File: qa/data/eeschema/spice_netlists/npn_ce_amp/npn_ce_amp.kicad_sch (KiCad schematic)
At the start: 10 parts

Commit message: Sim: Bugfixes, mostly for MS Windows compilation errors
Unfortunately, Windows headers define a lot of macros for common words,
so we had to rename some enums to not collide.

We also fix some of the many bugs related to the new simulation
architecture and the Spice Model Editor dialog.
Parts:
- Q1: Model_Device NPN -> (none); Model_Library npn.lib.spice -> (none); Model_Name NPN -> (none); Model_Pins 1 2 3 -> (none); Model_Type GUMMELPOON -> (none); Sim_Device (none) -> NPN; Sim_Library (none) -> npn.lib.spice; Sim_Name (none) -> NPN; Sim_Pins (none) -> 1 2 3; Sim_Type (none) -> GUMMELPOON
- V1: Model_Device V -> (none); Model_Params dc=9 -> (none); Model_Pins 1 2 -> (none); Model_Type DC -> (none); Sim_Device (none) -> V; Sim_Params (none) -> dc=9; Sim_Pins (none) -> 1 2; Sim_Type (none) -> DC
- V2: Model_Device V -> (none); Model_Params dc=0 ampl=10m f=10k -> (none); Model_Pins 1 2 -> (none); Model_Type SIN -> (none); Sim_Device (none) -> V; Sim_Params (none) -> dc=0 ampl=10m f=10k; Sim_Pins (none) -> 1 2; Sim_Type (none) -> SIN
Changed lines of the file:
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@@
       (effects (font (size 1.27 1.27)) hide)
     )
-    (property "Model_Name" "NPN" (id 4) (at 142.875 92.71 0)
+    (property "Sim_Name" "NPN" (id 4) (at 142.875 92.71 0)
       (effects (font (size 1.27 1.27)))
     )
-    (property "Model_Library" "npn.lib.spice" (id 5) (at 135.89 88.9 0)
+    (property "Sim_Library" "npn.lib.spice" (id 5) (at 135.89 88.9 0)
       (effects (font (size 1.27 1.27)) hide)
     )
-    (property "Model_Device" "NPN" (id 6) (at 135.89 88.9 0)
+    (property "Sim_Device" "NPN" (id 6) (at 135.89 88.9 0)
       (effects (font (size 1.27 1.27)) hide)
     )
-    (property "Model_Type" "GUMMELPOON" (id 7) (at 135.89 88.9 0)
+    (property "Sim_Type" "GUMMELPOON" (id 7) (at 135.89 88.9 0)
       (effects (font (size 1.27 1.27)) hide)
     )
-    (property "Model_Pins" "1 2 3" (id 8) (at 135.89 88.9 0)
+    (property "Sim_Pins" "1 2 3" (id 8) (at 135.89 88.9 0)
       (effects (font (size 1.27 1.27)) hide)
     )
@@
       (effects (font (size 1.27 1.27)) hide)
     )
-    (property "Model_Device" "V" (id 4) (at 114.3 93.98 0)
+    (property "Sim_Device" "V" (id 4) (at 114.3 93.98 0)
       (effects (font (size 1.27 1.27)) hide)
     )
-    (property "Model_Type" "SIN" (id 5) (at 114.3 93.98 0)
+    (property "Sim_Type" "SIN" (id 5) (at 114.3 93.98 0)
       (effects (font (size 1.27 1.27)) hide)
     )
-    (property "Model_Pins" "1 2" (id 6) (at 114.3 93.98 0)
+    (property "Sim_Pins" "1 2" (id 6) (at 114.3 93.98 0)
       (effects (font (size 1.27 1.27)) hide)
     )
-    (property "Model_Params" "dc=0 ampl=10m f=10k" (id 7) (at 114.3 106.68 0)
+    (property "Sim_Params" "dc=0 ampl=10m f=10k" (id 7) (at 114.3 106.68 0)
       (effects (font (size 1.27 1.27)))
     )
@@
       (effects (font (size 1.27 1.27)) hide)
     )
-    (property "Model_Device" "V" (id 4) (at 101.6 85.09 0)
+    (property "Sim_Device" "V" (id 4) (at 101.6 85.09 0)
       (effects (font (size 1.27 1.27)) hide)
     )
-    (property "Model_Type" "DC" (id 5) (at 101.6 85.09 0)
+    (property "Sim_Type" "DC" (id 5) (at 101.6 85.09 0)
       (effects (font (size 1.27 1.27)) hide)
     )
-    (property "Model_Pins" "1 2" (id 6) (at 101.6 85.09 0)
+    (property "Sim_Pins" "1 2" (id 6) (at 101.6 85.09 0)
       (effects (font (size 1.27 1.27)) hide)
     )
-    (property "Model_Params" "dc=9" (id 7) (at 107.95 87.63 0)
+    (property "Sim_Params" "dc=9" (id 7) (at 107.95 87.63 0)
       (effects (font (size 1.27 1.27)))
     )

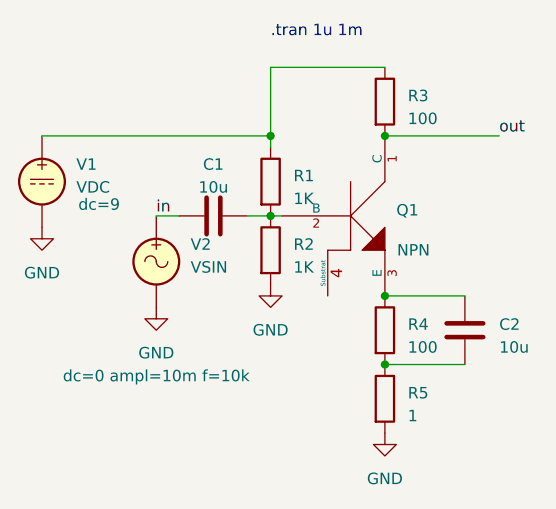
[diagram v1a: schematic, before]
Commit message: Sim: Only store device type in reference, not full model type
Instead of Reference="VSIN1", Value="dc=1 ampl=2 f=3", it's now
Reference="V1", Value="SIN dc=1 ampl=2 f=3".
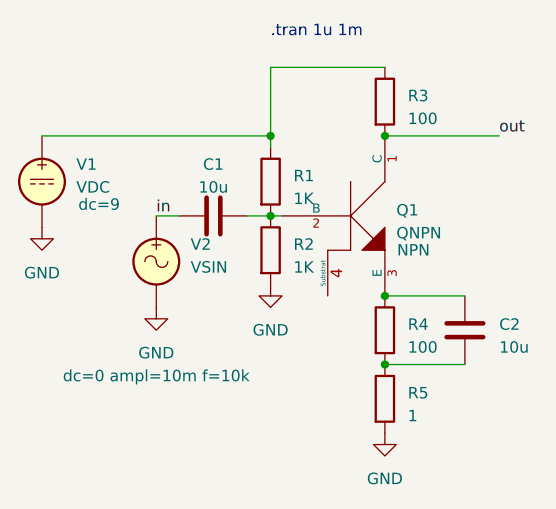
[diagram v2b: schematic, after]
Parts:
- Q1: value (none) -> QNPN
- V1: Sim_Type DC -> (none)

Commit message: Sim: Remove inference from Reference and Value
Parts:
- C1, C2: Sim_Device (none) -> C
- R1, R2, R3, R4, R5: Sim_Device (none) -> R
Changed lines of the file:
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@@
+      (effects (font (size 1.27 1.27)) hide)
+    )
+    (property "Sim_Device" "C" (at 120.65 88.9 90)
       (effects (font (size 1.27 1.27)) hide)
     )
@@
       (effects (font (size 1.27 1.27)) hide)
     )
+    (property "Sim_Device" "C" (at 148.59 101.6 0)
+      (effects (font (size 1.27 1.27)) hide)
+    )
     (pin "1")
     (pin "2")
@@
     )
     (property "Datasheet" "~" (at 139.7 76.2 0)
+      (effects (font (size 1.27 1.27)) hide)
+    )
+    (property "Sim_Device" "R" (at 139.7 76.2 0)
       (effects (font (size 1.27 1.27)) hide)
     )
@@
       (effects (font (size 1.27 1.27)) hide)
     )
+    (property "Sim_Device" "R" (at 139.7 101.6 0)
+      (effects (font (size 1.27 1.27)) hide)
+    )
     (pin "1")
     (pin "2")
@@
       (effects (font (size 1.27 1.27)) hide)
     )
+    (property "Sim_Device" "R" (at 127 85.09 0)
+      (effects (font (size 1.27 1.27)) hide)
+    )
     (pin "1")
     (pin "2")
@@
       (effects (font (size 1.27 1.27)) hide)
     )
+    (property "Sim_Device" "R" (at 139.7 109.22 0)
+      (effects (font (size 1.27 1.27)) hide)
+    )
     (pin "1")
     (pin "2")
@@
       (effects (font (size 1.27 1.27)) hide)
     )
+    (property "Sim_Device" "R" (at 127 92.71 0)
+      (effects (font (size 1.27 1.27)) hide)
+    )

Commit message: Sim: Rename Sim_* fields to Sim.*
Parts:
- C1, C2: Sim_Device C -> (none)
- Q1: Sim_Device NPN -> (none); Sim_Pins 1 2 3 -> (none); Sim_Type GUMMELPOON -> (none)
- R1, R2, R3, R4, R5: Sim_Device R -> (none)
- V1: Sim_Device V -> (none); Sim_Params dc=9 -> (none); Sim_Pins 1 2 -> (none)
- V2: Sim_Device V -> (none); Sim_Params dc=0 ampl=10m f=10k -> (none); Sim_Pins 1 2 -> (none); Sim_Type SIN -> (none)
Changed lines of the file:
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@@
       (effects (font (size 1.27 1.27)) hide)
     )
-    (property "Sim_Device" "C" (at 120.65 88.9 90)
+    (property "Sim.Device" "C" (at 120.65 88.9 90)
       (effects (font (size 1.27 1.27)) hide)
     )
@@
       (effects (font (size 1.27 1.27)) hide)
     )
-    (property "Sim_Device" "NPN" (at 135.89 88.9 0)
-      (effects (font (size 1.27 1.27)) hide)
-    )
-    (property "Sim_Type" "GUMMELPOON" (at 135.89 88.9 0)
-      (effects (font (size 1.27 1.27)) hide)
-    )
-    (property "Sim_Pins" "1 2 3" (at 135.89 88.9 0)
+    (property "Sim.Device" "NPN" (at 135.89 88.9 0)
+      (effects (font (size 1.27 1.27)) hide)
+    )
+    (property "Sim.Type" "GUMMELPOON" (at 135.89 88.9 0)
+      (effects (font (size 1.27 1.27)) hide)
+    )
+    (property "Sim.Pins" "1 2 3" (at 135.89 88.9 0)
       (effects (font (size 1.27 1.27)) hide)
     )
@@
       (effects (font (size 1.27 1.27)) hide)
     )
-    (property "Sim_Device" "C" (at 148.59 101.6 0)
+    (property "Sim.Device" "C" (at 148.59 101.6 0)
       (effects (font (size 1.27 1.27)) hide)
     )
@@
       (effects (font (size 1.27 1.27)) hide)
     )
-    (property "Sim_Device" "R" (at 139.7 76.2 0)
+    (property "Sim.Device" "R" (at 139.7 76.2 0)
       (effects (font (size 1.27 1.27)) hide)
     )
@@
       (effects (font (size 1.27 1.27)) hide)
     )
-    (property "Sim_Device" "V" (at 114.3 93.98 0)
-      (effects (font (size 1.27 1.27)) hide)
-    )
-    (property "Sim_Type" "SIN" (at 114.3 93.98 0)
-      (effects (font (size 1.27 1.27)) hide)
-    )
-    (property "Sim_Pins" "1 2" (at 114.3 93.98 0)
-      (effects (font (size 1.27 1.27)) hide)
-    )
-    (property "Sim_Params" "dc=0 ampl=10m f=10k" (at 114.3 106.68 0)
+    (property "Sim.Device" "V" (at 114.3 93.98 0)
+      (effects (font (size 1.27 1.27)) hide)
+    )
+    (property "Sim.Type" "SIN" (at 114.3 93.98 0)
+      (effects (font (size 1.27 1.27)) hide)
+    )
+    (property "Sim.Pins" "1 2" (at 114.3 93.98 0)
+      (effects (font (size 1.27 1.27)) hide)
+    )
+    (property "Sim.Params" "dc=0 ampl=10m f=10k" (at 114.3 106.68 0)
       (effects (font (size 1.27 1.27)))
     )
@@
       (effects (font (size 1.27 1.27)) hide)
     )
-    (property "Sim_Device" "R" (at 139.7 101.6 0)
+    (property "Sim.Device" "R" (at 139.7 101.6 0)
       (effects (font (size 1.27 1.27)) hide)
     )
@@
       (effects (font (size 1.27 1.27)) hide)
     )
-    (property "Sim_Device" "R" (at 127 85.09 0)
+    (property "Sim.Device" "R" (at 127 85.09 0)
       (effects (font (size 1.27 1.27)) hide)
     )
@@
       (effects (font (size 1.27 1.27)) hide)
     )
-    (property "Sim_Device" "R" (at 139.7 109.22 0)
+    (property "Sim.Device" "R" (at 139.7 109.22 0)
       (effects (font (size 1.27 1.27)) hide)
     )
@@
       (effects (font (size 1.27 1.27)) hide)
     )
-    (property "Sim_Device" "R" (at 127 92.71 0)
+    (property "Sim.Device" "R" (at 127 92.71 0)
       (effects (font (size 1.27 1.27)) hide)
     )
@@
       (effects (font (size 1.27 1.27)) hide)
     )
-    (property "Sim_Device" "V" (at 101.6 85.09 0)
-      (effects (font (size 1.27 1.27)) hide)
-    )
-    (property "Sim_Pins" "1 2" (at 101.6 85.09 0)
-      (effects (font (size 1.27 1.27)) hide)
-    )
-    (property "Sim_Params" "dc=9" (at 107.95 87.63 0)
-      (effects (font (size 1.27 1.27)))
-    )
+    (property "Sim.Device" "V" (at 101.6 85.09 0)
+      (effects (font (size 1.27 1.27)) hide)
+    )
+    (property "Sim.Pins" "1 2" (at 101.6 85.09 0)
+      (effects (font (size 1.27 1.27)) hide)
+    )
+    (property "Sim.Params" "dc=9" (at 107.95 87.63 0)
+      (effects (font (size 1.27 1.27)))
+    )

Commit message: Sim: Rename the missed Sim_* fields to Sim.*
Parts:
- Q1: Sim_Library npn.lib.spice -> (none); Sim_Name NPN -> (none)
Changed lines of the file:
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@@
       (effects (font (size 1.27 1.27)) hide)
     )
-    (property "Sim_Name" "NPN" (at 142.875 92.71 0)
+    (property "Sim.Name" "NPN" (at 142.875 92.71 0)
       (effects (font (size 1.27 1.27)))
     )
-    (property "Sim_Library" "npn.lib.spice" (at 135.89 88.9 0)
+    (property "Sim.Library" "npn.lib.spice" (at 135.89 88.9 0)
       (effects (font (size 1.27 1.27)) hide)
     )
